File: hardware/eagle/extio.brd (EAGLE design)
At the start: 66 x 52 mm, 50 parts, among them IC1 PCF8574P, Q1 IRLZ44N, Q2 IRLZ44N, Q3 IRLZ44N, Q4 IRLZ44N, Q5 IRLZ44N, Q6 IRLZ44N, Q7 IRLZ44N, Q8 IRLZ44N

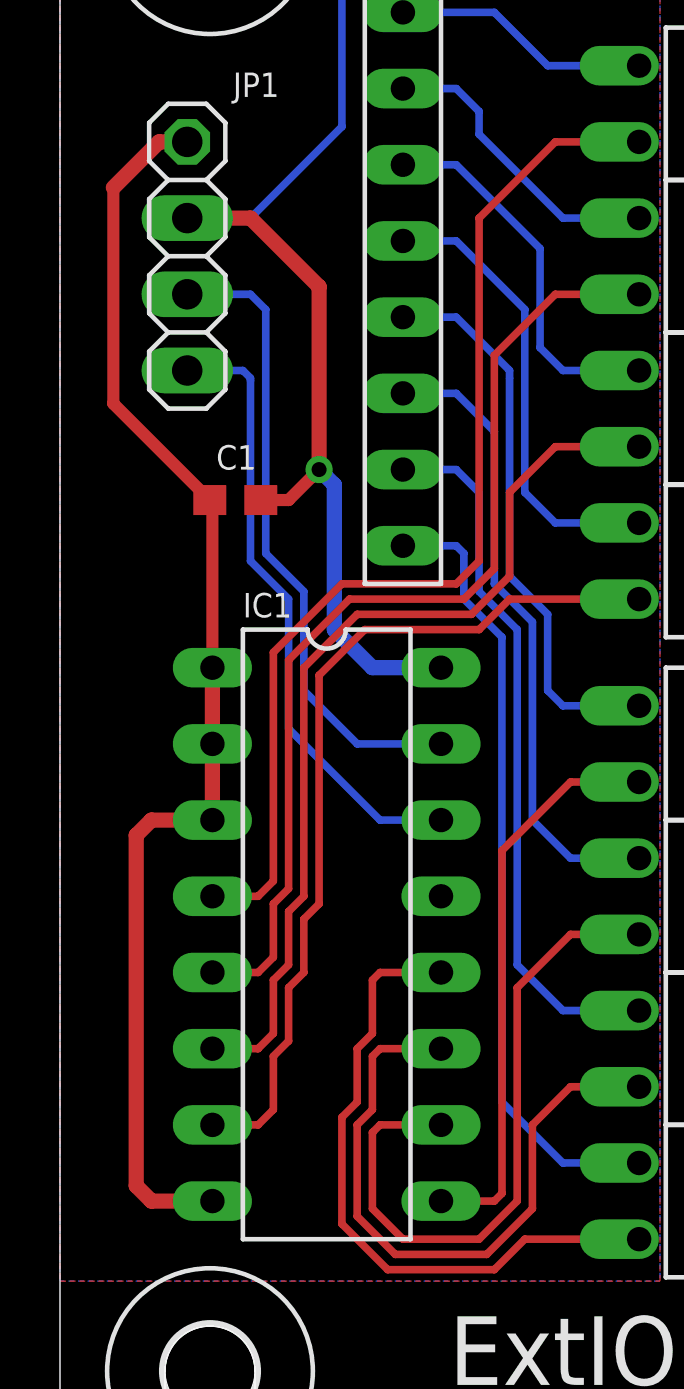
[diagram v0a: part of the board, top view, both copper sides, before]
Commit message: ExtIO A0..A1: jmp1..jmp2
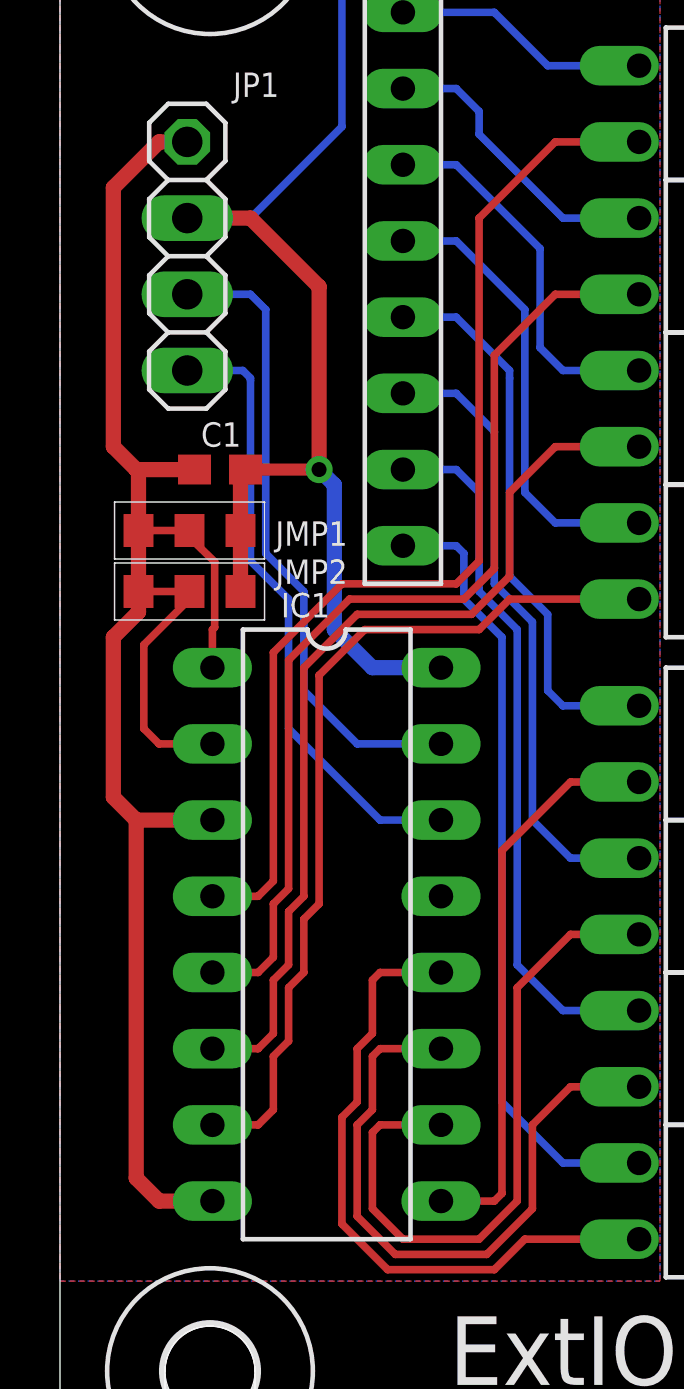
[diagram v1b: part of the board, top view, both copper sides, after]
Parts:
- added JMP1, JMP2: 0R-JUMP0603-ACLOSED, gate433:JMP0603-ACLOSED
- moved C1 1.14 mm to (5.33, 35.1)
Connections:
- removed net N$71: C1.2, IC1.1, IC1.2, IC1.3, IC1.8, JP1.1
- new net N$1: C1.2, IC1.3, IC1.8, JMP1.A, JMP2.A, JP1.1
- new net N$2: IC1.1, JMP1.C
- new net N$3: IC1.2, JMP2.C
- net N$69: now also JMP1.B, JMP2.B
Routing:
- net N$1: track 0.00 -> 44.5 mm
- net N$71: track 42.7 -> 0.00 mm
- net N$3: track 0.00 -> 7.70 mm
- net N$2: track 0.00 -> 4.96 mm
- net N$69: track 37.0 -> 41.3 mm
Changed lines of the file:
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@@
 <layer number="46" name="Milling" color="3" fill="1" visible="no" active="yes"/>
 <layer number="47" name="Measures" color="7" fill="1" visible="yes" active="yes"/>
-<layer number="48" name="Document" color="7" fill="1" visible="no" active="yes"/>
+<layer number="48" name="Document" color="7" fill="1" visible="yes" active="yes"/>
 <layer number="49" name="Reference" color="7" fill="1" visible="no" active="yes"/>
 <layer number="50" name="dxf" color="7" fill="1" visible="no" active="no"/>
@@
 <wire x1="3.5" y1="55" x2="0" y2="55" width="0" layer="20"/>
 <wire x1="0" y1="55" x2="0" y2="3" width="0" layer="20"/>
-<dimension x1="0" y1="3" x2="66" y2="3" x3="33" y3="-6" textsize="1.778" layer="47"/>
-<dimension x1="5" y1="5" x2="40" y2="5" x3="22.5" y3="-2" textsize="1.778" layer="47"/>
-<dimension x1="5" y1="53" x2="5" y2="5" x3="-5" y3="29" textsize="1.778" layer="47"/>
+<dimension x1="0" y1="3" x2="66" y2="3" x3="33" y3="-6" textsize="1.778" layer="48"/>
+<dimension x1="5" y1="5" x2="40" y2="5" x3="22.5" y3="-2" textsize="1.778" layer="48"/>
+<dimension x1="5" y1="53" x2="5" y2="5" x3="-5" y3="29" textsize="1.778" layer="48"/>
 <text x="12.97" y="4.54" size="2.286" layer="21" font="vector" ratio="10">ExtIO v1.0</text>
 <text x="32.512" y="39.37" size="0.8128" layer="21" font="vector">+   -</text>
-<dimension x1="0" y1="55" x2="0" y2="3" x3="-9.906" y3="29" textsize="1.778" layer="47"/>
+<dimension x1="0" y1="55" x2="0" y2="3" x3="-9.906" y3="29" textsize="1.778" layer="48"/>
 <wire x1="3.5" y1="55" x2="3.5" y2="53" width="0" layer="20"/>
 <wire x1="3.5" y1="53" x2="6.5" y2="53" width="0" layer="20" curve="180"/>
@@
 <attribute name="MPN" value="PCF8574PN" x="8.89" y="19.558" size="1.778" layer="27" rot="R270" display="off"/>
 <attribute name="OC_NEWARK" value="11N8515" x="8.89" y="19.558" size="1.778" layer="27" rot="R270" display="off"/>
-<attribute name="NAME" x="6.096" y="30.1244" size="0.8128" layer="25" font="vector" ratio="10"/>
+<attribute name="NAME" x="7.366" y="30.1244" size="0.8128" layer="25" font="vector" ratio="10"/>
 <attribute name="VALUE" x="7.9248" y="28.448" size="1.778" layer="27" ratio="10" rot="R270"/>
 </element>
@@
 <element name="U$3" library="gate433" package="3,0" value="" x="40" y="5" locked="yes" smashed="yes"/>
 <element name="U$4" library="gate433" package="3,0" value="" x="40" y="53" locked="yes" smashed="yes"/>
-<element name="C1" library="resistor" package="C0603" value="1uF" x="5.842" y="34.036" smashed="yes" rot="R180">
-<attribute name="NAME" x="5.207" y="35.052" size="0.8128" layer="25" font="vector" ratio="10"/>
-<attribute name="VALUE" x="3.683" y="35.941" size="1.27" layer="27" ratio="10" rot="R180"/>
-<attribute name="SPICEPREFIX" value="C" x="5.842" y="34.036" size="1.778" layer="27" rot="R180" display="off"/>
+<element name="C1" library="resistor" package="C0603" value="1uF" x="5.334" y="35.052" smashed="yes" rot="R180">
+<attribute name="NAME" x="4.699" y="35.814" size="0.8128" layer="25" font="vector" ratio="10"/>
+<attribute name="VALUE" x="3.175" y="36.957" size="1.27" layer="27" ratio="10" rot="R180"/>
+<attribute name="SPICEPREFIX" value="C" x="5.334" y="35.052" size="1.778" layer="27" rot="R180" display="off"/>
+</element>
+<element name="JMP1" library="gate433" package="JMP0603-ACLOSED" value="0R-JUMP0603-ACLOSED" x="4.318" y="33.02" smashed="yes">
+<attribute name="NAME" x="8.382" y="32.512" size="0.8128" layer="25" font="vector" ratio="10" align="bottom-center"/>
+<attribute name="VALUE" x="4.318" y="30.861" size="0.8128" layer="27" align="bottom-center"/>
+</element>
+<element name="JMP2" library="gate433" package="JMP0603-ACLOSED" value="0R-JUMP0603-ACLOSED" x="4.318" y="30.988" smashed="yes">
+<attribute name="NAME" x="8.382" y="31.242" size="0.8128" layer="25" font="vector" ratio="10" align="bottom-center"/>
+<attribute name="VALUE" x="4.318" y="28.829" size="0.8128" layer="27" align="bottom-center"/>
 </element>
 </elements>
@@
 <wire x1="8.636" y1="41.148" x2="6.35" y2="43.434" width="0.508" layer="1"/>
 <wire x1="6.35" y1="43.434" x2="4.2418" y2="43.434" width="0.508" layer="1"/>
-<wire x1="6.692" y1="34.036" x2="7.62" y2="34.036" width="0.4064" layer="1"/>
-<wire x1="7.62" y1="34.036" x2="8.636" y2="35.052" width="0.4064" layer="1"/>
+<wire x1="6.184" y1="35.052" x2="8.636" y2="35.052" width="0.4064" layer="1"/>
+<contactref element="JMP2" pad="B"/>
+<contactref element="JMP1" pad="B"/>
+<wire x1="6.018" y1="30.988" x2="6.018" y2="33.02" width="0.508" layer="1"/>
+<wire x1="6.018" y1="33.02" x2="6.018" y2="34.886" width="0.508" layer="1"/>
+<wire x1="6.018" y1="34.886" x2="6.184" y2="35.052" width="0.508" layer="1"/>
 </signal>
 <signal name="N$71">
-<contactref element="IC1" pad="1"/>
-<contactref element="IC1" pad="2"/>
-<contactref element="IC1" pad="3"/>
-<contactref element="IC1" pad="8"/>
-<contactref element="JP1" pad="1"/>
-<contactref element="C1" pad="2"/>
-<wire x1="4.2418" y1="45.974" x2="3.302" y2="45.974" width="0.508" layer="1"/>
-<wire x1="3.302" y1="45.974" x2="1.778" y2="44.45" width="0.508" layer="1"/>
-<wire x1="5.08" y1="28.448" x2="5.08" y2="25.908" width="0.508" layer="1"/>
-<wire x1="5.08" y1="25.908" x2="5.08" y2="23.368" width="0.508" layer="1"/>
-<wire x1="5.08" y1="23.368" x2="3.048" y2="23.368" width="0.508" layer="1"/>
-<wire x1="3.048" y1="23.368" x2="2.54" y2="22.86" width="0.508" layer="1"/>
-<wire x1="2.54" y1="22.86" x2="2.54" y2="11.176" width="0.508" layer="1"/>
-<wire x1="2.54" y1="11.176" x2="3.048" y2="10.668" width="0.508" layer="1"/>
-<wire x1="3.048" y1="10.668" x2="5.08" y2="10.668" width="0.508" layer="1"/>
 <polygon width="0.4064" layer="16" isolate="0.6096">
 <vertex x="0" y="55"/>
@@
 <vertex x="20" y="8"/>
 </polygon>
-<wire x1="1.778" y1="44.45" x2="1.778" y2="37.25" width="0.4064" layer="1"/>
-<wire x1="1.778" y1="37.25" x2="4.992" y2="34.036" width="0.4064" layer="1"/>
-<wire x1="5.08" y1="28.448" x2="5.08" y2="33.948" width="0.4064" layer="1"/>
-<wire x1="5.08" y1="33.948" x2="4.992" y2="34.036" width="0.4064" layer="1"/>
+</signal>
+<signal name="N$1">
+<contactref element="JP1" pad="1"/>
+<contactref element="C1" pad="2"/>
+<contactref element="JMP1" pad="A"/>
+<contactref element="IC1" pad="8"/>
+<contactref element="JMP2" pad="A"/>
+<contactref element="IC1" pad="3"/>
+<wire x1="4.2418" y1="45.974" x2="3.302" y2="45.974" width="0.508" layer="1"/>
+<wire x1="3.302" y1="45.974" x2="1.778" y2="44.45" width="0.508" layer="1"/>
+<wire x1="1.778" y1="44.45" x2="1.778" y2="35.814" width="0.508" layer="1"/>
+<wire x1="1.778" y1="35.814" x2="2.54" y2="35.052" width="0.508" layer="1"/>
+<wire x1="2.54" y1="35.052" x2="4.484" y2="35.052" width="0.508" layer="1"/>
+<wire x1="2.618" y1="33.02" x2="2.618" y2="34.974" width="0.508" layer="1"/>
+<wire x1="2.618" y1="34.974" x2="2.54" y2="35.052" width="0.508" layer="1"/>
+<wire x1="2.618" y1="30.988" x2="2.618" y2="33.02" width="0.508" layer="1"/>
+<wire x1="2.618" y1="30.988" x2="2.618" y2="30.304" width="0.508" layer="1"/>
+<wire x1="2.618" y1="30.304" x2="1.778" y2="29.464" width="0.508" layer="1"/>
+<wire x1="1.778" y1="29.464" x2="1.778" y2="24.13" width="0.508" layer="1"/>
+<wire x1="5.08" y1="10.668" x2="3.302" y2="10.668" width="0.508" layer="1"/>
+<wire x1="3.302" y1="10.668" x2="2.54" y2="11.43" width="0.508" layer="1"/>
+<wire x1="2.54" y1="11.43" x2="2.54" y2="23.368" width="0.508" layer="1"/>
+<wire x1="1.778" y1="24.13" x2="2.54" y2="23.368" width="0.508" layer="1"/>
+<wire x1="5.08" y1="23.368" x2="2.54" y2="23.368" width="0.508" layer="1"/>
+</signal>
+<signal name="N$2">
+<contactref element="JMP1" pad="C"/>
+<contactref element="IC1" pad="1"/>
+<wire x1="4.318" y1="33.02" x2="4.318" y2="32.7914" width="0.254" layer="1"/>
+<wire x1="4.318" y1="32.7914" x2="5.1562" y2="31.9786" width="0.254" layer="1"/>
+<wire x1="5.1562" y1="31.9786" x2="5.1562" y2="29.7942" width="0.254" layer="1"/>
+<wire x1="5.1562" y1="29.7942" x2="5.08" y2="29.718" width="0.254" layer="1"/>
+<wire x1="5.08" y1="29.718" x2="5.08" y2="28.448" width="0.254" layer="1"/>
+</signal>
+<signal name="N$3">
+<contactref element="JMP2" pad="C"/>
+<contactref element="IC1" pad="2"/>
+<wire x1="4.318" y1="30.988" x2="4.318" y2="30.734" width="0.254" layer="1"/>
+<wire x1="4.318" y1="30.734" x2="2.794" y2="29.21" width="0.254" layer="1"/>
+<wire x1="2.794" y1="29.21" x2="2.794" y2="26.416" width="0.254" layer="1"/>
+<wire x1="2.794" y1="26.416" x2="3.302" y2="25.908" width="0.254" layer="1"/>
+<wire x1="3.302" y1="25.908" x2="5.08" y2="25.908" width="0.254" layer="1"/>
 </signal>
 </signals>
